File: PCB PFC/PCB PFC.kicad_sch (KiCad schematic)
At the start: 44 parts, among them J1 INA_1, J2 INA_2, J4 External_Power, J5 BAT54S_1, J6 BAT54S_2, SW2 SW_Push, U2 L7805, U3 TL082, U4 TL084, U5 TL082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

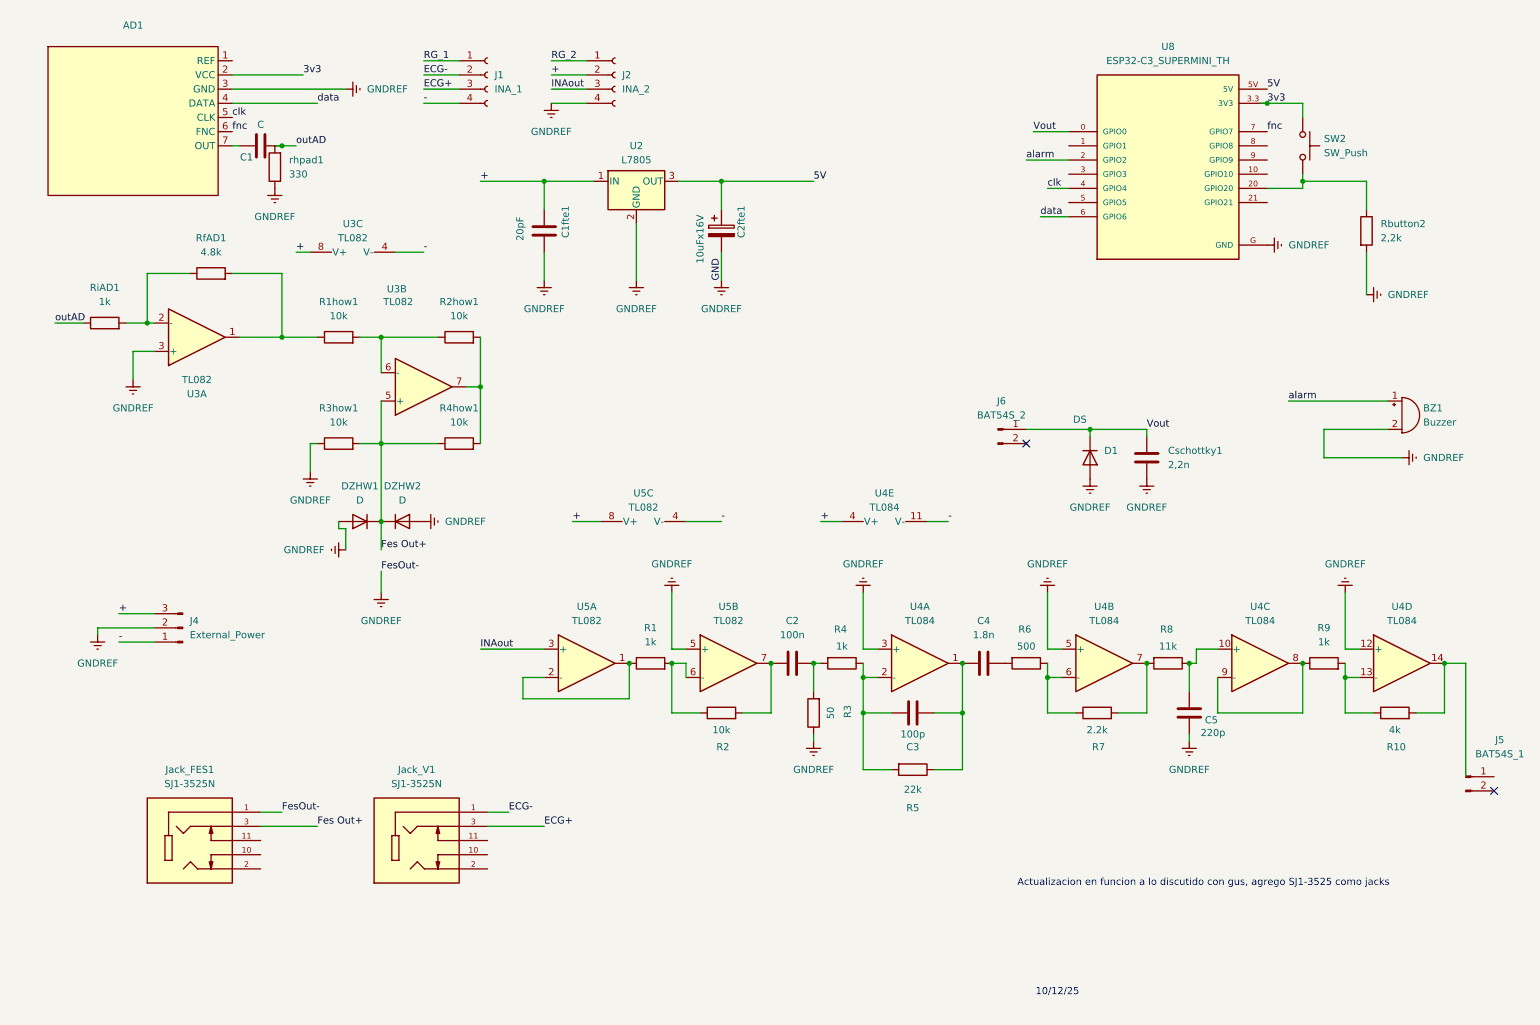
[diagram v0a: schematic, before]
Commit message: Cambio valores a comerciales y agrego OpAmps SMD
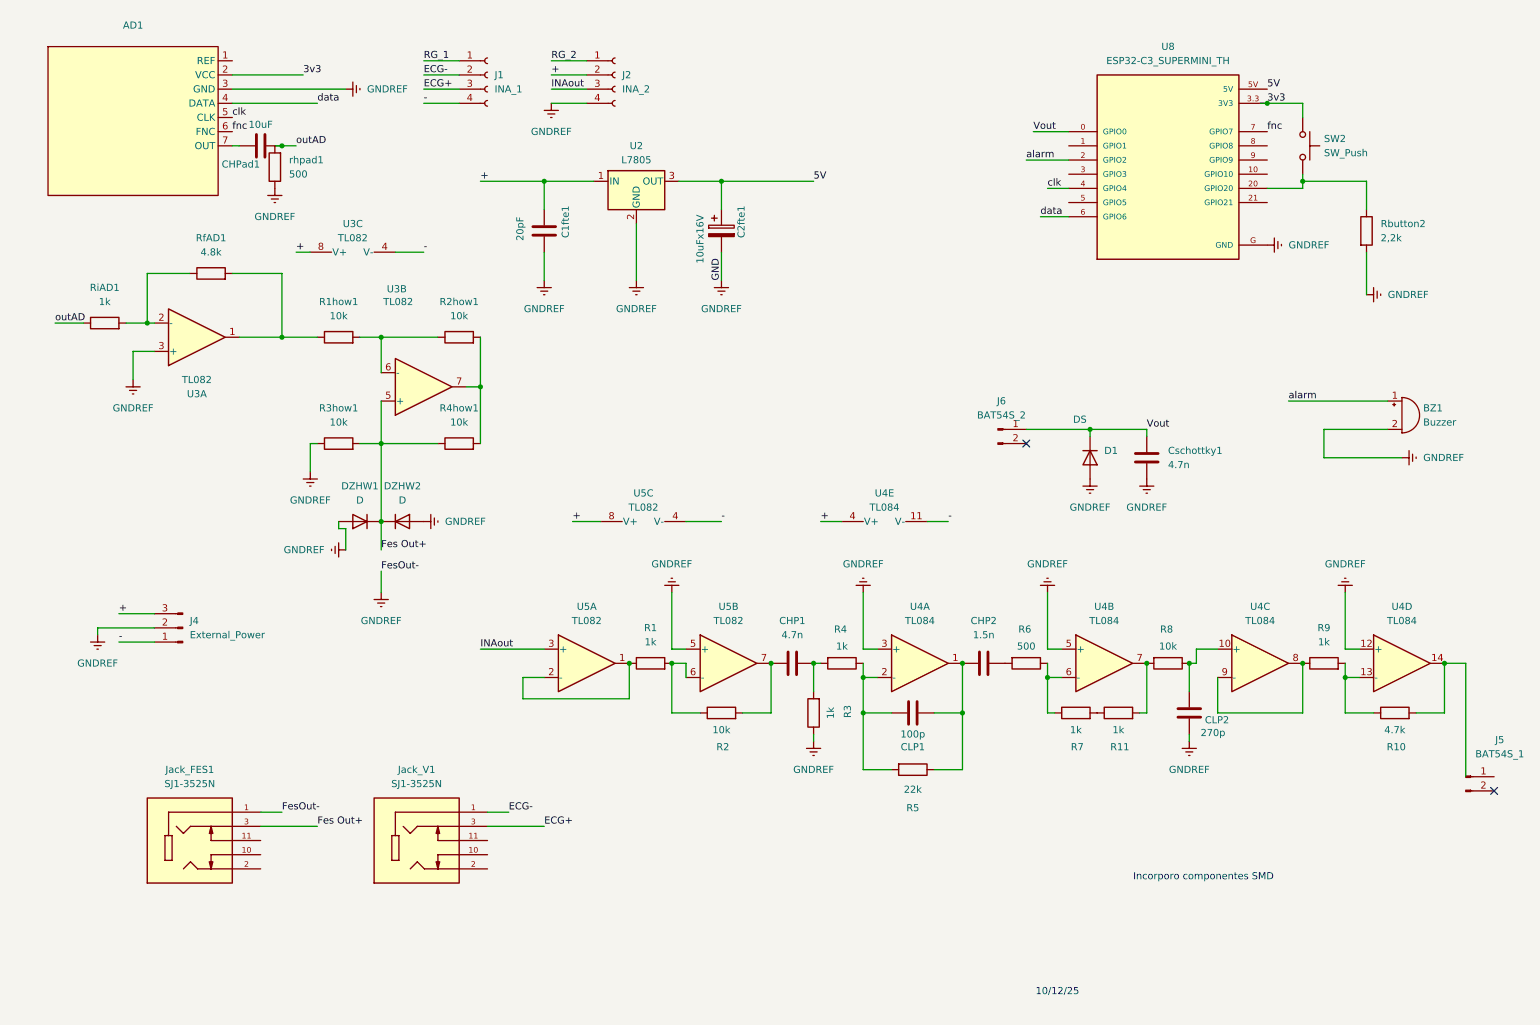
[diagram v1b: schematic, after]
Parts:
- added R11: 1k, Resistor_SMD:R_0805_2012Metric, symbol Device:R
- C1fte1: footprint Capacitor_THT:C_Disc_D5.0mm_W2.5mm_P2.50mm -> Capacitor_SMD:C_0603_1608Metric
- C2fte1: footprint Capacitor_THT:CP_Radial_D5.0mm_P2.50mm -> Capacitor_SMD:C_0805_2012Metric
- CHP1: renamed from C2; value 100n -> 4.7n; footprint Capacitor_THT:C_Disc_D5.0mm_W2.5mm_P2.50mm -> Capacitor_SMD:C_0603_1608Metric
- CHP2: renamed from C4; value 1.8n -> 1.5n; footprint Capacitor_THT:C_Disc_D5.0mm_W2.5mm_P2.50mm -> Capacitor_SMD:C_0603_1608Metric
- CHPad1: renamed from C1; value C -> 10uF; footprint Capacitor_THT:C_Disc_D5.0mm_W2.5mm_P2.50mm -> Capacitor_SMD:C_0603_1608Metric
- CLP1: renamed from C3; footprint Capacitor_THT:C_Disc_D5.0mm_W2.5mm_P2.50mm -> Capacitor_SMD:C_0603_1608Metric
- CLP2: renamed from C5; value 220p -> 270p; footprint Capacitor_THT:C_Disc_D5.0mm_W2.5mm_P2.50mm -> Capacitor_SMD:C_0603_1608Metric
- Cschottky1: value 2,2n -> 4.7n; footprint Capacitor_THT:C_Disc_D5.0mm_W2.5mm_P2.50mm -> Capacitor_SMD:C_0603_1608Metric
- R1, R1how1, R2, R2how1, R3how1, R4, R4how1, R5, R6, R9, Rbutton2, RfAD1, RiAD1: footprint Resistor_THT:R_Axial_DIN0204_L3.6mm_D1.6mm_P7.62mm_Horizontal -> Resistor_SMD:R_0805_2012Metric
- R10: value 4k -> 4.7k; footprint Resistor_THT:R_Axial_DIN0204_L3.6mm_D1.6mm_P7.62mm_Horizontal -> Resistor_SMD:R_0805_2012Metric
- R3: value 50 -> 1k; footprint Resistor_THT:R_Axial_DIN0204_L3.6mm_D1.6mm_P7.62mm_Horizontal -> Resistor_SMD:R_0805_2012Metric
- R7: value 2.2k -> 1k; footprint Resistor_THT:R_Axial_DIN0204_L3.6mm_D1.6mm_P7.62mm_Horizontal -> Resistor_SMD:R_0805_2012Metric
- R8: value 11k -> 10k; footprint Resistor_THT:R_Axial_DIN0204_L3.6mm_D1.6mm_P7.62mm_Horizontal -> Resistor_SMD:R_0805_2012Metric
- U3, U5: footprint Package_DIP:DIP-8_W7.62mm -> Package_SO:SOIC-8_3.9x4.9mm_P1.27mm
- U4: footprint Package_DIP:DIP-14_W7.62mm -> Package_SO:SOIC-14_3.9x8.7mm_P1.27mm
- rhpad1: value 330 -> 500; footprint Resistor_THT:R_Axial_DIN0204_L3.6mm_D1.6mm_P7.62mm_Horizontal -> Resistor_SMD:R_0805_2012Metric
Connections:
- net at R8.2, U4.7: now also R11.2; no longer R7.2
- new net: R11.1, R7.2
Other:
- note added: "Incorporo componentes SMD"
- note removed: "Actualizacion en funcion a lo discutido con gus, agrego SJ1-3525 como jacks"
- moved on the sheet: R7

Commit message: Placa final chidori 3V3 by Gus
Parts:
- removed BZ1: Buzzer, Buzzer_Beeper:Buzzer_12x9.5RM7.6, symbol Device:Buzzer
- removed C1fte1: 20pF, Capacitor_SMD:C_0603_1608Metric, symbol Device:C
- removed C2fte1: 10uFx16V, Capacitor_SMD:C_0805_2012Metric, symbol Device:C_Polarized
- removed J1: INA_1, Connector_PinSocket_2.54mm:PinSocket_1x04_P2.54mm_Vertical, symbol Connector:Conn_01x04_Socket
- removed J2: INA_2, Connector_PinSocket_2.54mm:PinSocket_1x04_P2.54mm_Vertical, symbol Connector:Conn_01x04_Socket
- removed J6: BAT54S_2, Connector_PinSocket_2.54mm:PinSocket_1x02_P2.54mm_Vertical, symbol Connector:Conn_01x02_Pin
- removed U2: L7805, Package_TO_SOT_THT:TO-220-3_Vertical, symbol Regulator_Linear:L7805
- added Cd_01, Cd_2, Cd_3, Cd_4, Cd_5, Cd_6, Cd_7, Cd_8: 22n, Capacitor_SMD:C_0603_1608Metric, symbol Device:C
- added D2: BAT54S, Package_TO_SOT_SMD:SOT-23, symbol Diode:BAT54S
- added U1: INA128, Package_TO_SOT_SMD:SOT-23-8, symbol Amplifier_Instrumentation:INA128
- J5: value BAT54S_1 -> JUMPER_BAT54S
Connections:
- net 5V is gone; now on net +: U8.5V
- net +: now also AD1.2 (VCC), SW2.1, Cd_01.2, Cd_3.2, Cd_6.2, Cd_7.2, U1.7 (V+)
- net -: now also Cd_2.2, Cd_4.2, Cd_5.2, Cd_8.2, U1.4 (V-)
- net ECG+: now also U1.3 (+)
- net ECG-: now also U1.2 (-)
- net GNDREF: now also Cd_01.1, Cd_2.1, Cd_3.1, Cd_4.1, Cd_5.1, Cd_6.1, Cd_7.1, Cd_8.1, U1.5 (Ref)
- net INAout: now also U1.6
- net RG_1: now also U1.1 (Rg)
- net RG_2: now also U1.8 (Rg)
- net Vout: now also D2.2 (K)
- net alarm: now also U8.5 (GPIO5); no longer U8.2 (GPIO2)
- net CON_BAT54S: now reaches J5.1 (Pin_1)
- net CON_BAT54S: now also D2.3 (COM)
- net SIN_BAT54S: now reaches J5.2 (Pin_2)
- net SIN_BAT54S: now also R10.2, U4.14
- removed net 3v3: AD1.2 (VCC), SW2.1, U8.3.3 (3V3)
- net Fes Out+ renamed FesOut+
- no-connect marks 2 -> 16
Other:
- note added: "ADQUISICIÓN"
- note added: "INYECCIÓN CORRIENTE"
- note added: "MICROPROCESADO Y TRANSMISIÓN"
- moved on the sheet: AD1, CHP1, CHP2, CHPad1, CLP1, CLP2, Cschottky1, D1, DZHW1, DZHW2, J4, J5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

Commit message: actualizacion de placa y filtrado: correccion de ad9833 e ina + filtrado
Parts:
- CLP1: value 100p -> 4.7n
- Cschottky1: value 4.7n -> 10n
- R10: value 4.7k -> 16.2k
- R4: value 1k -> 337
- R5: value 22k -> 500
- U1: footprint Package_TO_SOT_SMD:SOT-23-8 -> Package_SO:SOIC-8_3.9x4.9mm_P1.27mm
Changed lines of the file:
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@@
 			)
 		)
-		(property "Footprint" "Package_TO_SOT_SMD:SOT-23-8"
+		(property "Footprint" "Package_SO:SOIC-8_3.9x4.9mm_P1.27mm"
 			(at 36.83 55.88 0)
 			(effects
@@
 			)
 		)
-		(property "Value" "22k"
+		(property "Value" "500"
 			(at 139.7 63.246 90)
 			(effects
@@
 			)
 		)
-		(property "Value" "4.7n"
+		(property "Value" "10n"
 			(at 269.24 72.3899 0)
 			(effects
@@
 			)
 		)
-		(property "Value" "4.7k"
+		(property "Value" "16.2k"
 			(at 226.06 52.578 90)
 			(effects
@@
 			)
 		)
-		(property "Value" "100p"
+		(property "Value" "4.7n"
 			(at 139.7 53.34 90)
 			(effects
@@
 			)
 		)
-		(property "Value" "1k"
+		(property "Value" "337"
 			(at 127 37.592 90)
 			(effects
